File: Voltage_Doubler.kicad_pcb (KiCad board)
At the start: 2 copper layers, 11 parts, among them J1 Conn_1x2, J2 Conn_1x2, U1 NE555D

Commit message: updated personal info
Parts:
- moved C1 542.6 mm to (163.5, 77.8)
- moved C2 542.6 mm to (161.2, 82.8)
- moved C3 542.6 mm to (146.0, 91.8)
- moved C4 542.6 mm to (154.5, 92.5)
- moved D1 542.6 mm to (138.3, 77.2)
- moved D2 542.6 mm to (148.6, 84.2)
- moved R1 542.6 mm to (137.4, 89.8)
- moved R2 542.6 mm to (142.5, 93.8)
- moved U1 542.6 mm to (153.9, 80.2)
- moved J1 541.4 mm to (170.1, 77.2), turned to 0 degrees
- moved J2 537.8 mm to (170.1, 92.2)
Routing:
- net GND: track 43.7 -> 0.00 mm
- net +5V: track 43.9 -> 49.0 mm
- net Net-(D2-K): track 34.7 -> 36.7 mm
- added copper zone on F.Cu, net GND

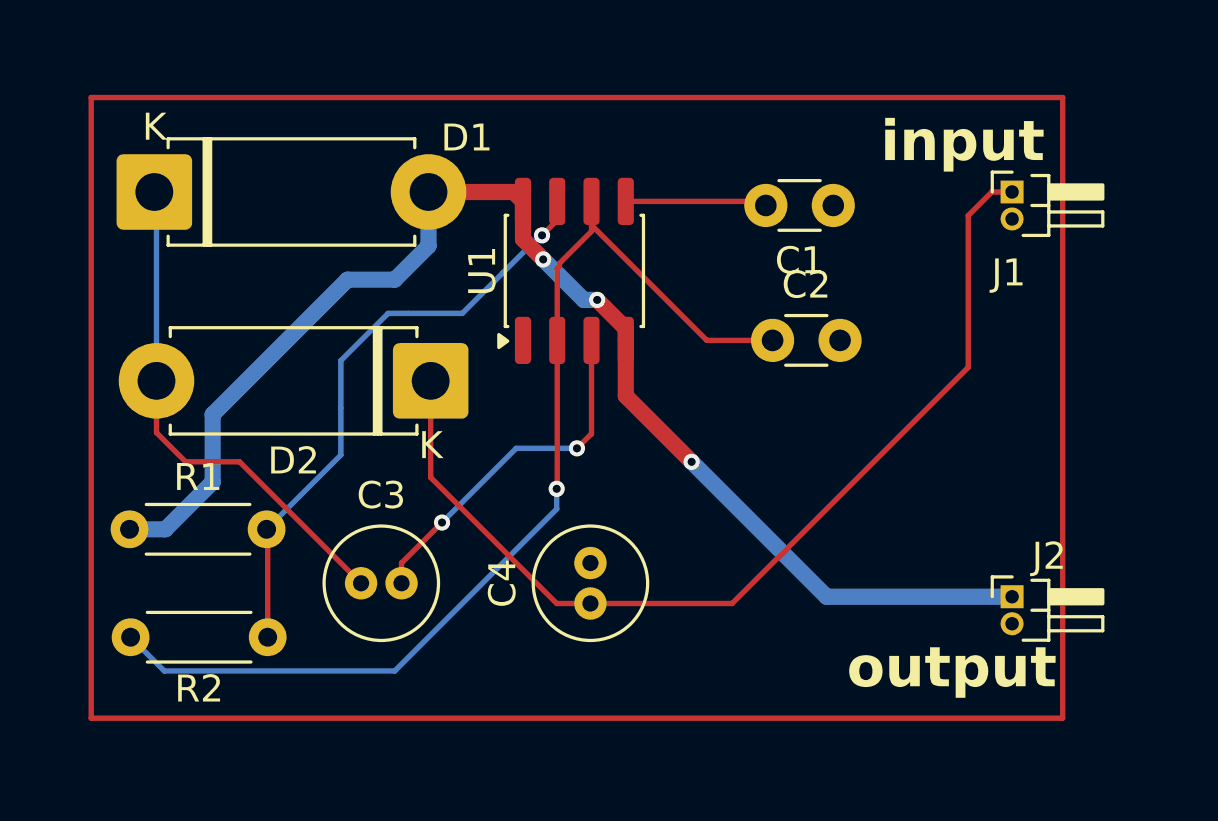
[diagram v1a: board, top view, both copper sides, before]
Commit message: Update: added front/back 2D views, copper fill views, schematic view, updated 3D views and PCB/schematic
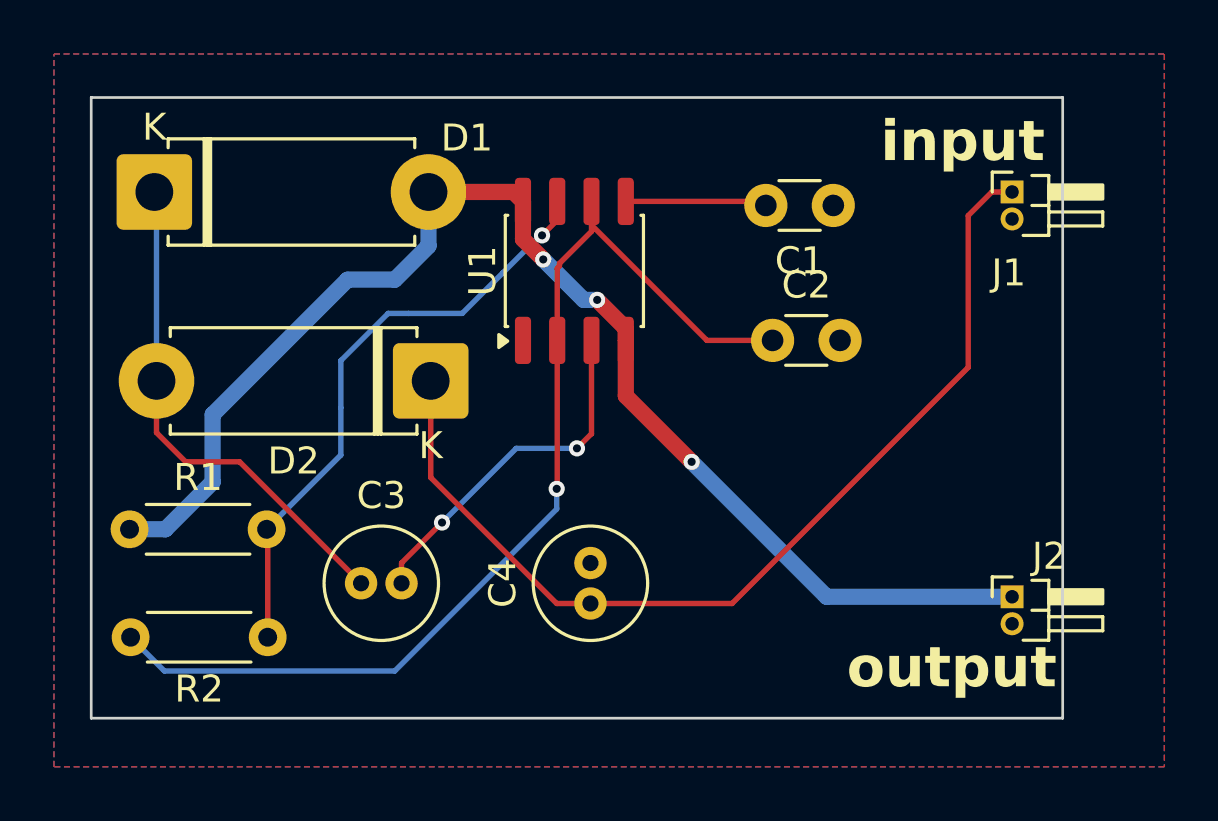
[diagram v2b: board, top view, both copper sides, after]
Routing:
- added copper zone on B.Cu, net GND
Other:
- board outline added: 36 x 23 mm
- board text added: "Voltage_Doubler 1.0 Ibrahim Jarallah"
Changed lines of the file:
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@@
 		(end 172 73.75)
 		(stroke
-			(width 0.2)
-			(type default)
-		)
-		(layer "F.Cu")
+			(width 0.1)
+			(type solid)
+		)
+		(layer "Edge.Cuts")
 	)
 	(gr_line
@@
 		(end 136 96.75)
 		(stroke
-			(width 0.2)
-			(type default)
-		)
-		(layer "F.Cu")
+			(width 0.1)
+			(type solid)
+		)
+		(layer "Edge.Cuts")
 	)
 	(gr_line
@@
 		(end 136 73.75)
 		(stroke
-			(width 0.2)
-			(type default)
-		)
-		(layer "F.Cu")
+			(width 0.1)
+			(type solid)
+		)
+		(layer "Edge.Cuts")
 	)
 	(gr_line
@@
 		(end 172 96.75)
 		(stroke
-			(width 0.2)
-			(type default)
-		)
-		(layer "F.Cu")
+			(width 0.1)
+			(type solid)
+		)
+		(layer "Edge.Cuts")
 	)
 	(gr_text "output"
@@
 		)
 	)
+	(gr_text "Voltage_Doubler\n1.0\nIbrahim Jarallah"
+		(at 160.02 86.106 0)
+		(layer "B.SilkS")
+		(effects
+			(font
+				(size 0.8 0.8)
+				(thickness 0.08)
+			)
+			(justify left bottom mirror)
+		)
+	)
 	(segment
 		(start 160.75 77.75)
@@
 		(net 1)
 		(net_name "GND")
-		(layer "F.Cu")
+		(layers "F.Cu" "B.Cu")
 		(hatch edge 0.5)
-		(connect_pads yes
+		(connect_pads
 			(clearance 0.5)
 		)
@@
 			(thermal_gap 0.5)
 			(thermal_bridge_width 0.5)
-			(island_removal_mode 1)
-			(island_area_min 10)
 		)
 		(polygon
 			(pts
-				(xy 136 73.75) (xy 172 73.75) (xy 172 96.75) (xy 136 96.75)
+				(xy 134.62 72.136) (xy 175.768 72.136) (xy 175.768 98.552) (xy 134.62 98.552)
 			)
 		)
